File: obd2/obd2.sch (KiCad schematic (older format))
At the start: 8 parts, among them U1 389-MCP2515-I/ST, U2 385-MCP2551-I/SN, U3 1389-LPC1343FBD48,151

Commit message: Moved some files around.
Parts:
- removed R?: R, ~, symbol R
- removed U1: 389-MCP2515-I/ST, Plecharts/axxkb, symbol 389-MCP2515-I/ST
- removed U3: 1389-LPC1343FBD48,151, melissa/dintu, symbol 1389-LPC1343FBD48,151
- added 0.1u, 0.33u: C, ~, symbol C
- added C? (x6): 0.1u, ~, symbol C
- added J?: RJ45, symbol RJ45
- added J?: MICRO_SD, symbol MICRO_SD
- added LCD?: LCD16X2, symbol LCD16X2
- added U?: 1449-LPC11C14FBD48/301,, melissa/dintu, symbol 1449-LPC11C14FBD48/301,
- added U?: LM7805, ~, symbol LM7805
- added U?: MCP1825S33, ~, symbol MCP1825S33
- added X?: CRYSTAL, ~, symbol CRYSTAL
- R? (x2): value R -> 60 Ohm
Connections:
- net labels added: CAN_RXD, CAN_TXD, VBAT
- net labels removed: CAN_CNTRL_CLKIN, CAN_CNTRL_CLKOUT_SOF, CAN_CNTRL_CS!, CAN_CNTRL_INT!, CAN_CNTRL_RESET!, CAN_CNTRL_RX0!, CAN_CNTRL_RX1!, CAN_CNTRL_TX0!, CAN_CNTRL_TX1!, CAN_CNTRL_TX2!
- wire segments 70 -> 60
- no-connect marks 1 -> 0
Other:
- note added: "XTAL required if C_CAN baud rates above 100kbit/s used"
- moved on the sheet: C?, R?

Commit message: Almost done schematic and component selections
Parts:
- removed J?: RJ45, symbol RJ45
- removed U2: 385-MCP2551-I/SN, Plecharts/b6cyy, symbol 385-MCP2551-I/SN
- removed U?: LM7805, ~, symbol LM7805
- removed U?: MCP1825S33, ~, symbol MCP1825S33
- added C2: 0.1uF, ~, symbol C
- added C7: 0.1u, ~, symbol C
- added D1: 3V3_ON, ~, symbol LED
- added J1: RJ45_BASIC, symbol RJ45_BASIC
- added JP1: LCD_V_SELECT, ~, symbol JUMPER3
- added MP1, MP2, MP3, MP4: SCREW_4-40, ~, symbol SCREW_4-40
- added P1: JTAG_PROG, symbol CONN_5X2
- added R1: 330R, ~, symbol R
- added R5: 4k7, ~, symbol R
- added R6, R7, R8: 10k, ~, symbol R
- added SW1, SW2, SW3: SW_OFF_MOM, ~, symbol SW_OFF_MOM
- added U1: SP7805, ~, symbol SP7805
- added U2: LM335, symbol LM335
- added U3: LD1117, symbol LD1117
- added U5: MCP2561, symbol MCP2561
- added W1: VBAT_T, symbol TEST
- added W2: 5V_T, symbol TEST
- added W3: 3V3_T, symbol TEST
- C1: renamed from 0.33u; value C -> 0.33uF
- C3: renamed from 0.1u; value C -> 0.1uF
- C4, C5: renamed from C?; value 0.1u -> 39pF
- C6: renamed from C?; value 0.1u -> 10uF
- X1: renamed from X?; value CRYSTAL -> 20MHz
- gave numbers to parts that had none: 10
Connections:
- net labels added: Button1, Button2, Button3, CARD_DETECT, LCD_DB4, LCD_DB5, LCD_DB6, LCD_DB7, LCD_E, LCD_RS, LCD_RW, SPI_SSEL, SWCLK, SWDIO, TEMP, UART_RXD, UART_TXD, ~RESET
- wire segments 60 -> 186
- no-connect marks 0 -> 10
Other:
- note added: "Mounting holes 4-40 hardware"
- moved on the sheet: C1, C11, C3, C6, C9, J2, LCD1, R2, R3, R4

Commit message: All signals routed but power
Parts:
- added C12, C13: 1u, ~, symbol C
- added D2: 1N4149, ~, symbol DIODE
- added F1: approx 300mA, ~, symbol FUSE
- added JP2: K_LINE, ~, symbol JUMPER
- added JP3: L_LINE, ~, symbol JUMPER
- added JP4: SCS, ~, symbol JUMPER
- added K1: UART, symbol CONN_3
- added LCD2: LCD_COG, symbol LCD_COG
- added P2: IO_1, symbol CONN_4
- added P3: IO_2, symbol CONN_6
- added R10: R_CON1, ~, symbol R
- added R11: R_CON2, ~, symbol R
- added R9: R_LCD_LED, ~, symbol R
- added SW4: PWR_SW, ~, symbol SWITCH_INV_MSM
- added W4: 12V_T, symbol TEST
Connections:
- net labels added: +12V, K_LINE, LCD_DB4/SCL, LCD_DB5/RST, LCD_E/CSB, LCD_RS/SI, LCD_RW/RS, L_LINE, SCS
- net labels removed: LCD_DB4, LCD_DB5, LCD_E, LCD_RS, LCD_RW
- wire segments 186 -> 275
- no-connect marks 10 -> 11
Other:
- note added: "1 2 3 4 5 6 7 8\n9 10 11 12 13 14 15 16"
- note added: "4 - Chassis Ground\n5 - Signal Ground\n6 - CAN high (J-2284)\n7 - K-LINE (ISO 9141-2 and ISO/DIS 14230-4)\n9 - SCS - (Service Check System - diagnostic codes)\n14 - CAN low\n15 - ISO 9141-2 L-Line (ISO 9141-2 and ISO/DIS 14230-4)\n16 - +12V unswitched"
- note added: "CAN transceiver circuitry"
- note added: "Micro-SD circuitry"
- note added: "OBD2 connection \nDLC - Diagnostic Link Connector in Honda Civic"
- note added: "Option for one of two types of LCD screen"
- note added: "R_CON1 and R_CON2 set contrast.\nR_LCD_LED sets LCD backlight brightness (10-30ohm)"
- note added: "Sensor circuitry"
- note added: "User input"
- note added: "VBAT is unswitched battery voltage\n+12V is switched/diode/fused\n+5V/+3.3V are regulated voltages"
- moved on the sheet: C7, J2, JP1, LCD1, R5, U2

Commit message: Routed power and added port for UART. Added logos.
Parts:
- removed U4: 1449-LPC11C14FBD48/301,, melissa/dintu, symbol 1449-LPC11C14FBD48/301,
- added U4: LPC11C14, symbol LPC11C14
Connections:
- wire segments 275 -> 278
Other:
- moved on the sheet: C6, C7, J2

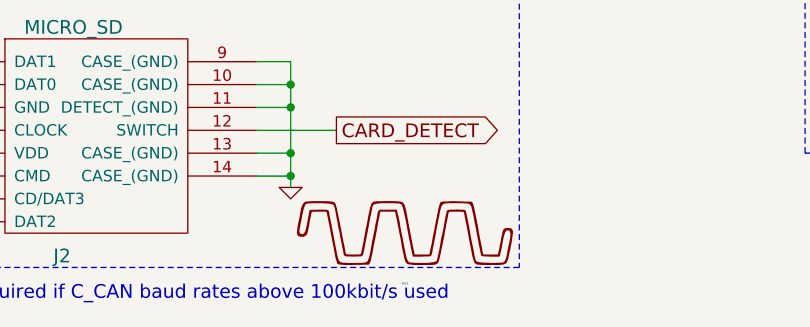
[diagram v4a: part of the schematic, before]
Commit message: Moved components to add enough room for 4-40 hardware. Moved all silkscreen values to appropriate places. rev 1 finished and ordered.
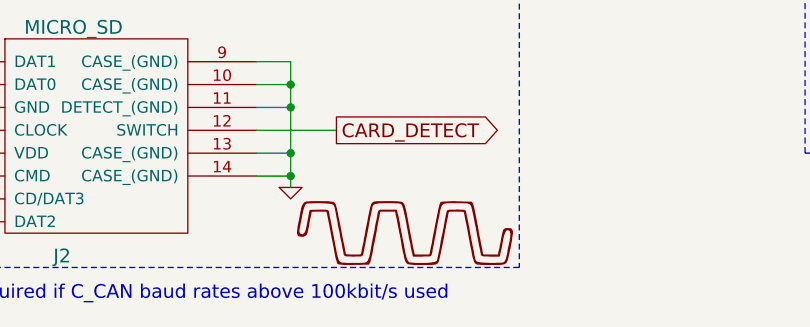
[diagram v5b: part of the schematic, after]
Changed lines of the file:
@@
 Sheet 1 1
 Title "obd2"
-Date "8 dec 2013"
+Date "31 dec 2013"
 Rev "1"
 Comp "Kevin Krieger"
@@
 23 FA 1C 2A F7 B2 F2 D1 4B 18 3D FE 3C 90 EC BE 9F 8C E4 BA 1C 4F F1 1E 2A C1 E7 57 2A 8E 42 61
 5B A6 4D BE 5D E0 40 5C EF 78 44 26 A1 19 E3 EE 1D D6 A0 F2 B0 FF A3 78 90 95 8F DD 58 D9 3E A0
-0D E7 FF 03 01 4C 61 85 B4 5B CE 3B 00 00 00 00 49 45 4E 44 AE 42 60 82 34 $EndBitmap
+0D E7 FF 03 01 4C 61 85 B4 5B CE 3B 00 00 00 00 49 45 4E 44 AE 42 60 82 00 $EndBitmap
 EndData
 $EndBitmap
@@
 U 1 1 52A3BE86
 P 5150 7650
-F 0 "#G1" H 5150 7430 10  0000 C CNN
+F 0 "#G1" H 5150 7430 10  0001 C CNN
 F 1 "LOGO" H 5150 7870 60  0001 C CNN
 F 2 "" H 5150 7650 60  0000 C CNN

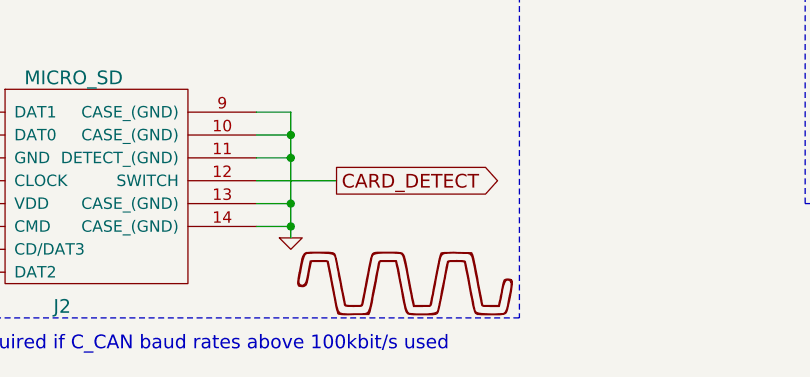
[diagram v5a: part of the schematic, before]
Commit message: Rearranged structure. added images.
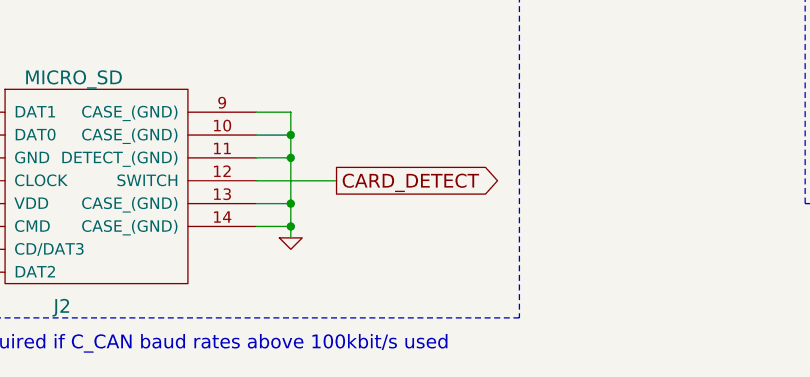
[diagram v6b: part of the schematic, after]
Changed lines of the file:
@@
 EndData
 $EndBitmap
-$Comp
-L LOGO #G1
-U 1 1 52A3BE86
-P 5150 7650
-F 0 "#G1" H 5150 7430 10  0001 C CNN
-F 1 "LOGO" H 5150 7870 60  0001 C CNN
-F 2 "" H 5150 7650 60  0000 C CNN
-F 3 "" H 5150 7650 60  0000 C CNN
-	1    5150 7650
-	1    0    0    -1
-$EndComp
 $EndSCHEMATC

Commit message: Added gitignore, added lpc usermanual, added BOM with comments
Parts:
- C1, C10, C11, C12, C13, C2, C3, C4, C5, C6, C7, C8, C9: footprint ~ -> c_0805
- D1: footprint ~ -> LED_J_LEAD
- D2: footprint ~ -> DO-35
- F1: footprint ~ -> SM0603
- J1: footprint (none) -> RJ45
- J2: footprint (none) -> SD_502702_003
- JP1: footprint ~ -> SOLDER_JUMPER_3
- JP2, JP3, JP4: footprint ~ -> SOLDER_JUMPER
- K1: footprint (none) -> SIL-3
- LCD1: footprint (none) -> GDM1602K
- LCD2: footprint (none) -> NHD_C0216CZ_NSW_BBW
- MP1, MP2, MP3, MP4: footprint ~ -> 1pin
- P1: footprint (none) -> GRPB052VWQS-RC
- P2: footprint (none) -> SIL-4
- P3: footprint (none) -> SIL-6
- R1, R10, R11, R2, R3, R4, R5, R6, R7, R8, R9: footprint ~ -> R3
- SW1, SW2, SW3: footprint ~ -> FSM4JSMA_pushbutton
- SW4: footprint ~ -> MMS1208
- U1: footprint ~ -> TO-252-3
- U2: footprint (none) -> TO92
- U3: footprint (none) -> DPAK
- U4: footprint (none) -> LQFP48
- U5: footprint (none) -> SOIC-8-Narrow
- W1, W2, W3, W4: footprint (none) -> SIL-2
- X1: footprint ~ -> CSM-3X
